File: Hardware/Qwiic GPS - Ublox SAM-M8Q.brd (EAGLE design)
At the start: 40.6 x 40.6 mm, 71 parts, among them J3 PTH, U2 SAM-M8Q

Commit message: Removing single unit files. Removing notes from schematic.
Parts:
- D1: value BLUE -> Yellow
- R11: value 470 -> 1k

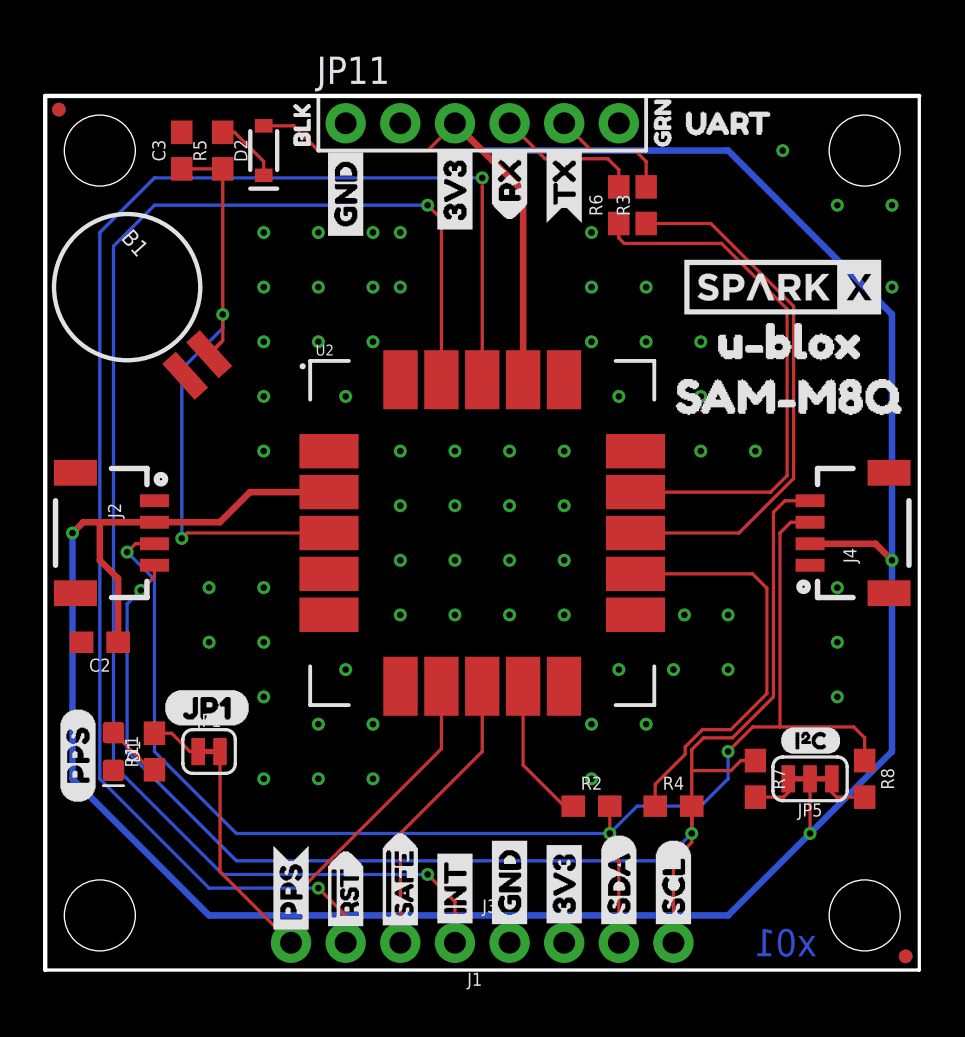
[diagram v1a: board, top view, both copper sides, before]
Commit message: Updated battery footprint
Footprint for the battery is now for the reflowable version
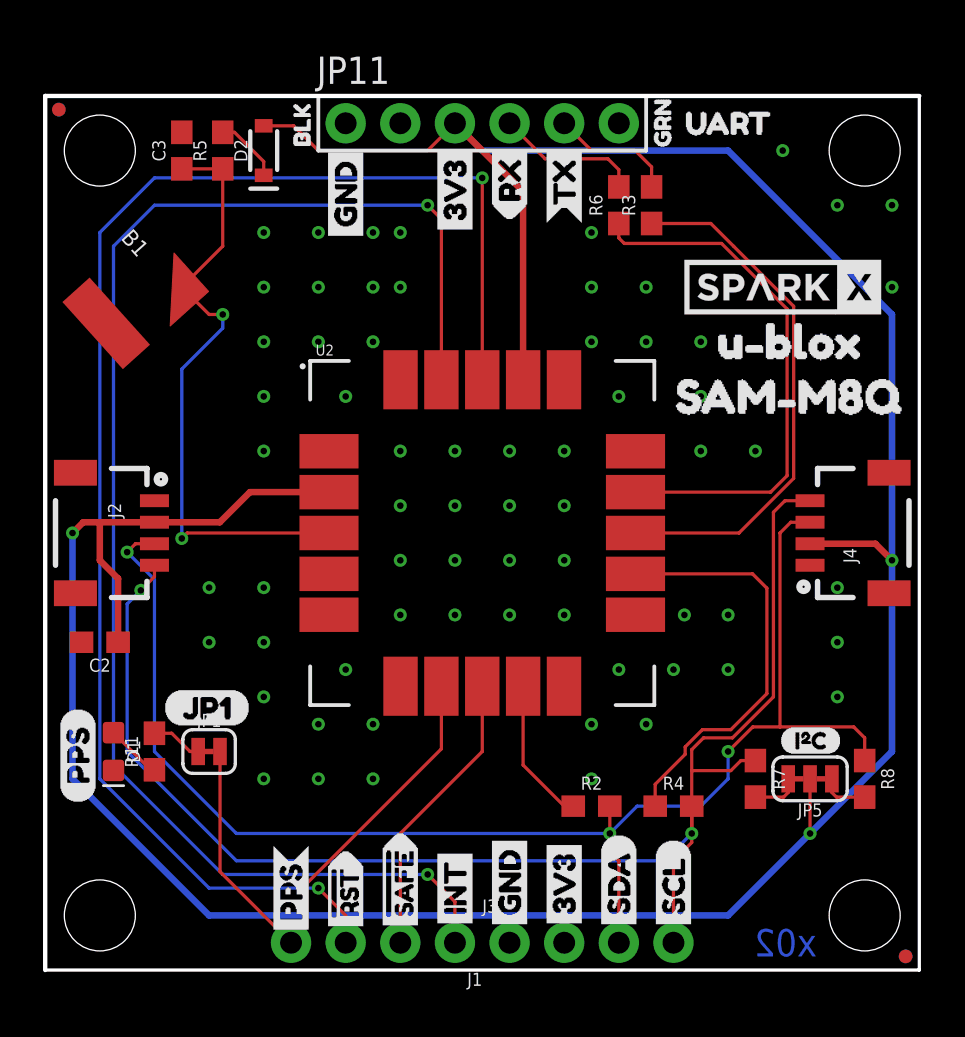
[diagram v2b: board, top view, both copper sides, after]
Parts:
- removed U$30: (no value), Labels:QWIIC-LOGO-MEDIUM
- added U$28: (no value), Labels:QWIIC-LOGO-LARGE
- B1: device SparkFun-Batteries:BATTCON-6.8MM -> SparkFun-Batteries:ML414H_IV01E
- moved R3 0.25 mm to (28.2, 35.6)
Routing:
- net BACKUP: track 29.8 -> 28.5 mm
- net 3.3V: track 150.2 -> 149.4 mm
- net SDA: track 68.0 -> 67.5 mm
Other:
- board text added: "x02"
- board text removed: "x01"
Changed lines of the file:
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@@
 <?xml version="1.0" encoding="utf-8"?>
 <!DOCTYPE eagle SYSTEM "eagle.dtd">
-<eagle version="9.2.1">
+<eagle version="9.3.0">
 <drawing>
 <settings>
@@
 <layer number="18" name="Vias" color="2" fill="1" visible="yes" active="yes"/>
 <layer number="19" name="Unrouted" color="6" fill="1" visible="yes" active="yes"/>
-<layer number="20" name="Dimension" color="24" fill="1" visible="yes" active="yes"/>
+<layer number="20" name="Dimension" color="15" fill="1" visible="yes" active="yes"/>
 <layer number="21" name="tPlace" color="16" fill="1" visible="yes" active="yes"/>
 <layer number="22" name="bPlace" color="14" fill="1" visible="yes" active="yes"/>
@@
 <wire x1="40.64" y1="40.64" x2="40.64" y2="0" width="0.1524" layer="20"/>
 <wire x1="40.64" y1="0" x2="0" y2="0" width="0.1524" layer="20"/>
-<text x="34.417" y="1.27" size="1.27" layer="16" font="vector" ratio="15" rot="MR180" align="center">x01</text>
+<text x="34.417" y="1.27" size="1.27" layer="16" font="vector" ratio="15" rot="MR180" align="center">x02</text>
 <text x="-2.54" y="-8.89" size="1.778" layer="47">Measurements in inches</text>
 <wire x1="12.7" y1="40.64" x2="12.7" y2="38.1" width="0.1778" layer="21"/>
@@
 <attribute name="VALUE" x="5.588" y="14.859" size="0.6096" layer="27" font="vector" ratio="20" rot="R180" align="top-center"/>
 </element>
-<element name="R3" library="SparkFun-Resistors" package="0603" value="470" x="27.94" y="35.56" smashed="yes" rot="R90">
-<attribute name="NAME" x="27.178" y="35.56" size="0.6096" layer="25" font="vector" ratio="20" rot="R90" align="bottom-center"/>
-<attribute name="PROD_ID" value="RES-07869" x="27.94" y="35.56" size="1.778" layer="27" font="vector" ratio="15" rot="R90" display="off"/>
-<attribute name="VALUE" value="470" x="27.686" y="33.274" size="0.6096" layer="27" font="vector" ratio="20" rot="R90" align="top-center"/>
+<element name="R3" library="SparkFun-Resistors" package="0603" value="470" x="28.194" y="35.56" smashed="yes" rot="R90">
+<attribute name="NAME" x="27.432" y="35.56" size="0.6096" layer="25" font="vector" ratio="20" rot="R90" align="bottom-center"/>
+<attribute name="PROD_ID" value="RES-07869" x="28.194" y="35.56" size="1.778" layer="27" font="vector" ratio="15" rot="R90" display="off"/>
+<attribute name="VALUE" value="470" x="27.94" y="33.274" size="0.6096" layer="27" font="vector" ratio="20" rot="R90" align="top-center"/>
 </element>
 <element name="R6" library="SparkFun-Resistors" package="0603" value="470" x="26.67" y="35.56" smashed="yes" rot="R90">
@@
 <attribute name="VALUE" x="6.223" y="35.433" size="0.6096" layer="27" font="vector" ratio="20" rot="R90" align="top-center"/>
 </element>
-<element name="B1" library="SparkFun-Batteries" package="BATTCON-6.8MM" value="6.8MM_COIN_CELL" x="3.81" y="31.75" smashed="yes" rot="R312">
+<element name="B1" library="SparkFun-Batteries" package="ML414H_IV01E" value="6.8MM_COIN_CELL" x="3.81" y="31.75" smashed="yes" rot="R312">
 <attribute name="NAME" x="3.479103125" y="34.015490625" size="0.762" layer="25" ratio="15" rot="R312"/>
-<attribute name="PROD_ID" value="BATT-13734" x="3.81" y="31.75" size="1.778" layer="27" rot="R312" display="off"/>
-<attribute name="VALUE" value="6.8MM_COIN_CELL" x="1.62684375" y="33.772034375" size="0.762" layer="27" ratio="15" rot="R312"/>
+<attribute name="PROD_ID" value="BATT-14267" x="3.81" y="31.75" size="1.778" layer="27" rot="R312" display="off"/>
 </element>
 <element name="R7" library="SparkFun-Resistors" package="0603" value="2.2k" x="33.02" y="8.89" smashed="yes" rot="R270">
@@
 <element name="U$25" library="buzzard_labels (5)" package="SAM#M8Q4" value="" x="41.021" y="26.67" smashed="yes" rot="MR0"/>
 <element name="U$29" library="buzzard_labels (6)" package="PPS0" value="" x="1.524" y="7.747" smashed="yes" rot="R90"/>
-<element name="U$30" library="Labels" package="QWIIC-LOGO-MEDIUM" value="" x="35.56" y="8.89" smashed="yes" rot="MR0"/>
 <element name="U$31" library="SparkX" package="SPARKX-MEDIUM" value="SPARKX-LOGO4" x="34.29" y="31.75" smashed="yes"/>
 <element name="U$2" library="SparkX" package="SPARKX-MEDIUM" value="SPARKX-LOGO4" x="34.29" y="31.75" smashed="yes" rot="MR0"/>
@@
 <element name="U$17" library="buzzard_labels (8)" package="GRN2" value="" x="28.702" y="37.592" smashed="yes" rot="MR90"/>
 <element name="U$18" library="buzzard_labels (8)" package="JP10" value="" x="5.461" y="12.192" smashed="yes"/>
+<element name="U$28" library="Labels" package="QWIIC-LOGO-LARGE" value="" x="35.56" y="8.89" smashed="yes" rot="MR0"/>
 </elements>
 <signals>
@@
 <wire x1="39.37" y1="19.05" x2="38.6" y2="19.82" width="0.3048" layer="1"/>
 <via x="39.37" y="19.05" extent="1-16" drill="0.3048"/>
-<wire x1="35.56" y1="19.82" x2="36.441" y2="19.82" width="0.1524" layer="1"/>
 <wire x1="24.13" y1="1.27" x2="24.13" y2="2.54" width="0.3048" layer="16"/>
 <wire x1="22.22" y1="27.445" x2="22.22" y2="36.2" width="0.3048" layer="1"/>
@@
 <via x="35.56" y="6.35" extent="1-16" drill="0.3048"/>
 </signal>
-<signal name="GND" airwireshidden="yes">
+<signal name="GND">
 <contactref element="J2" pad="1"/>
 <contactref element="J3" pad="1"/>
@@
 <wire x1="26.25" y1="6.35" x2="26.25" y2="5.5" width="0.1524" layer="1"/>
 <wire x1="26.25" y1="5.5" x2="26.67" y2="5.08" width="0.1524" layer="1"/>
-<wire x1="26.67" y1="7.62" x2="26.25" y2="8.04" width="0.1524" layer="1"/>
 <wire x1="38.1" y1="9.74" x2="38.1" y2="10.795" width="0.1524" layer="1"/>
 <wire x1="37.592" y1="11.303" x2="34.163" y2="11.303" width="0.1524" layer="1"/>
@@
 <wire x1="34.798" y1="30.861" x2="32.004" y2="33.655" width="0.1524" layer="1"/>
 <wire x1="27.445" y1="20.32" x2="32.258" y2="20.32" width="0.1524" layer="1"/>
-<wire x1="27.94" y1="34.71" x2="30.948996875" y2="34.71" width="0.1524" layer="1"/>
+<wire x1="28.194" y1="34.71" x2="30.948996875" y2="34.71" width="0.1524" layer="1"/>
 </signal>
 <signal name="RXLV">
@@
 <via x="8.255" y="30.48" extent="1-16" drill="0.3048"/>
 <wire x1="8.255" y1="37.25" x2="6.35" y2="37.25" width="0.1524" layer="1"/>
-<wire x1="8.255" y1="37.25" x2="8.255" y2="30.48" width="0.1524" layer="1"/>
-<wire x1="7.626021875" y1="28.63273125" x2="8.255" y2="29.261709375" width="0.1524" layer="1"/>
 <wire x1="6.35" y1="27.94" x2="8.255" y2="29.845" width="0.1524" layer="16"/>
 <wire x1="8.255" y1="30.48" x2="8.255" y2="29.845" width="0.1524" layer="16"/>
-<wire x1="8.203290625" y1="29.21" x2="7.626021875" y2="28.63273125" width="0.1524" layer="1"/>
-<wire x1="8.255" y1="29.261709375" x2="8.255" y2="30.48" width="0.1524" layer="1"/>
 <wire x1="13.195" y1="20.32" x2="6.604" y2="20.32" width="0.1524" layer="1"/>
 <wire x1="6.604" y1="20.32" x2="6.35" y2="20.066" width="0.1524" layer="1"/>
+<wire x1="8.255" y1="30.48" x2="7.62" y2="30.48" width="0.1524" layer="1"/>
+<wire x1="7.62" y1="30.48" x2="6.67305" y2="31.42695" width="0.1524" layer="1"/>
+<wire x1="6.67305" y1="31.42695" x2="6.67305" y2="31.607034375" width="0.254" layer="1"/>
+<wire x1="6.67305" y1="31.607034375" x2="6.67305" y2="32.07305" width="0.254" layer="1"/>
+<wire x1="8.255" y1="33.655" x2="8.255" y2="37.25" width="0.1524" layer="1"/>
+<wire x1="6.67305" y1="32.07305" x2="8.255" y2="33.655" width="0.1524" layer="1"/>
 </signal>
 <signal name="INT">
@@
 <wire x1="24.13" y1="39.37" x2="25.4" y2="38.1" width="0.1524" layer="1"/>
 <wire x1="25.4" y1="38.1" x2="27.432" y2="38.1" width="0.1524" layer="1"/>
-<wire x1="27.94" y1="37.592" x2="27.432" y2="38.1" width="0.1524" layer="1"/>
-<wire x1="27.94" y1="36.41" x2="27.94" y2="37.592" width="0.1524" layer="1"/>
+<wire x1="28.194" y1="37.338" x2="27.432" y2="38.1" width="0.1524" layer="1"/>
+<wire x1="28.194" y1="36.41" x2="28.194" y2="37.338" width="0.1524" layer="1"/>
 </signal>
 </signals>
@@
 <mfgpreviewcolor name="substratecolor" color="0xFF786E46"/>
 </mfgpreviewcolors>
+<errors>
+</errors>
 </board>
 </drawing>
